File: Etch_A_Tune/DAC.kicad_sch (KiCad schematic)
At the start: 1 part, among them IC2 TLV320DAC3100IRHBR

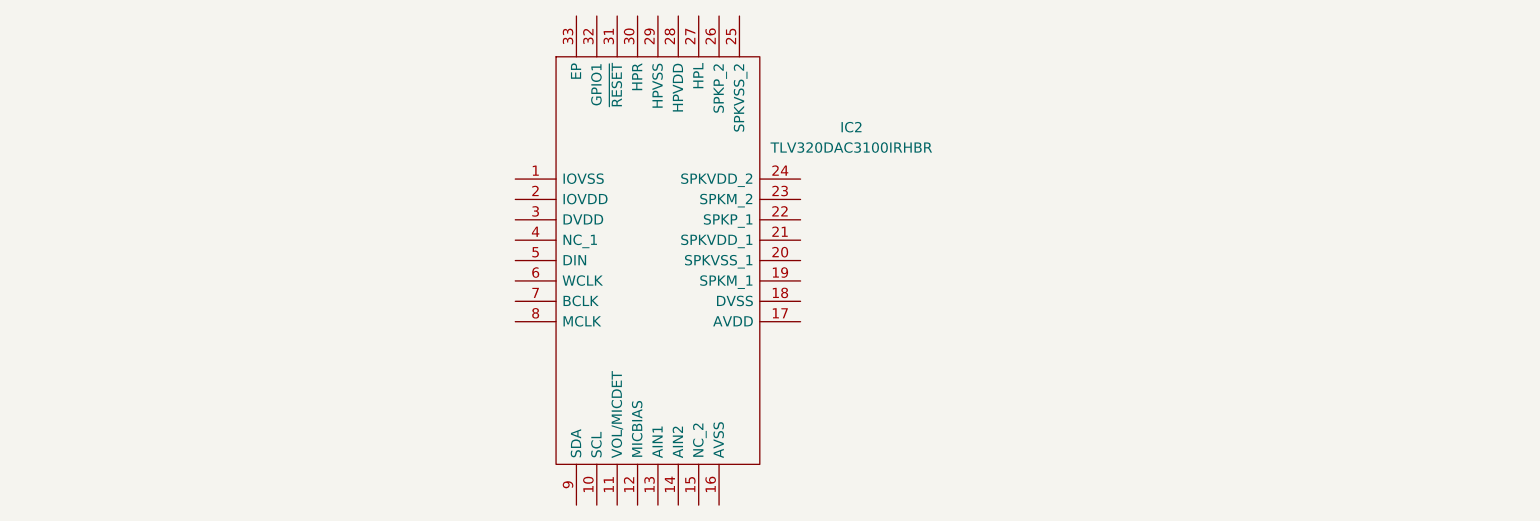
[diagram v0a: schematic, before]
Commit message: Updated schematic and preliminary PCB doc
did rough PCB layout
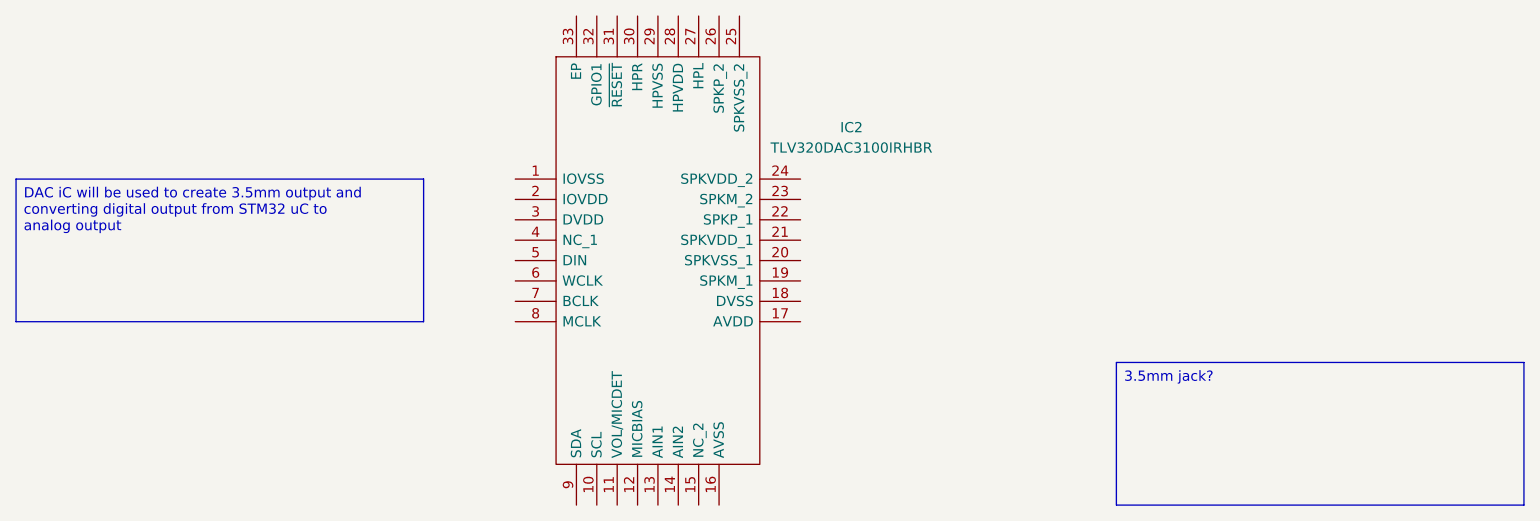
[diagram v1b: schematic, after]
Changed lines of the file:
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@@
 	(generator_version "9.0")
 	(paper "A4")
+	(text_box "DAC iC will be used to create 3.5mm output and converting digital output from STM32 uC to analog output"
+		(exclude_from_sim no)
+		(at 55.88 81.28 0)
+		(size 50.8 17.78)
+		(margins 0.9525 0.9525 0.9525 0.9525)
+		(stroke
+			(width 0)
+			(type solid)
+		)
+		(fill
+			(type none)
+		)
+		(effects
+			(font
+				(size 1.27 1.27)
+			)
+			(justify left top)
+		)
+	)
+	(text_box "3.5mm jack?\n"
+		(exclude_from_sim no)
+		(at 193.04 104.14 0)
+		(size 50.8 17.78)
+		(margins 0.9525 0.9525 0.9525 0.9525)
+		(stroke
+			(width 0)
+			(type solid)
+		)
+		(fill
+			(type none)
+		)
+		(effects
+			(font
+				(size 1.27 1.27)
+			)
+			(justify left top)
+		)
+	)
 	(symbol
 		(lib_id "SamacSys_Parts:TLV320DAC3100IRHBR")

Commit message: Schematic Update
Fixed component Footprints and added new switches/rotary encoders. Wired and placed bypass capacitors for most devices. Removed 5V boost converter because external DAC is no longer being utilized. Placed uC onto board design and implemented charging through USB-C connector.
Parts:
- removed IC2: TLV320DAC3100IRHBR, QFN50P500X500X100-33N-D, symbol SamacSys_Parts:TLV320DAC3100IRHBR
